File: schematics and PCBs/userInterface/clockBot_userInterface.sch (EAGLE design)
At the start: 7 parts

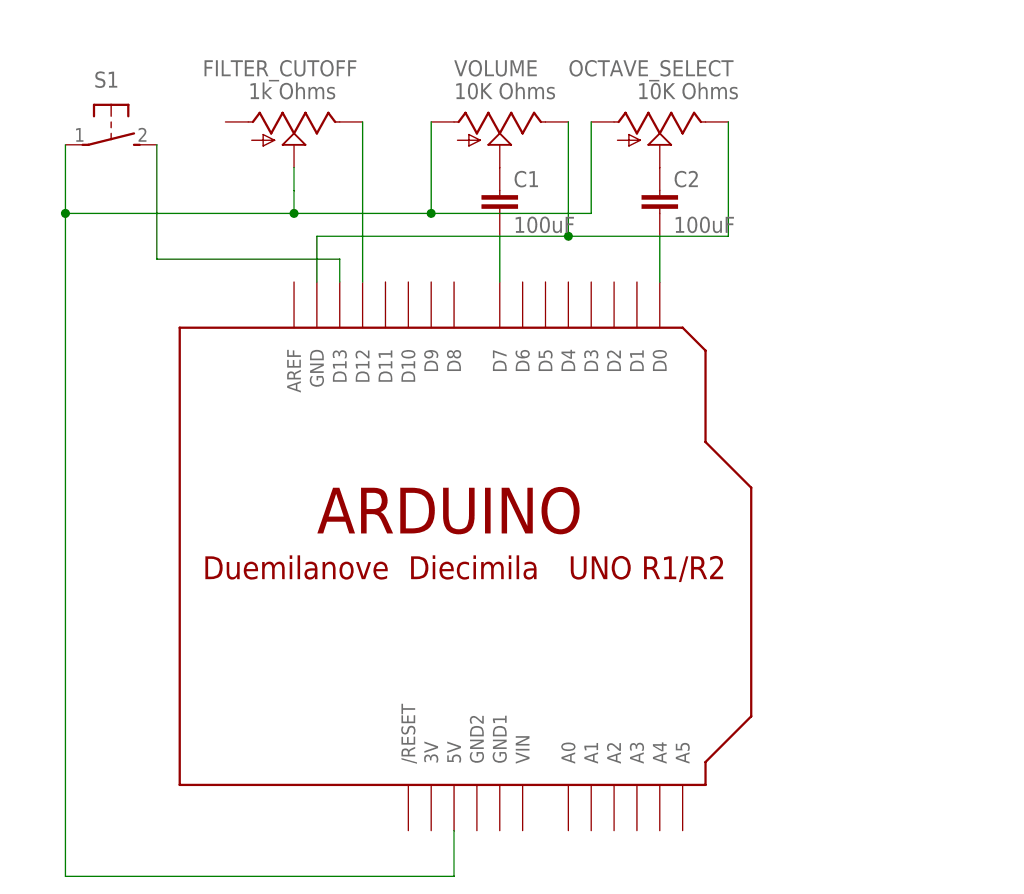
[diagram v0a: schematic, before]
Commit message: organized folders and added erin grace schematic
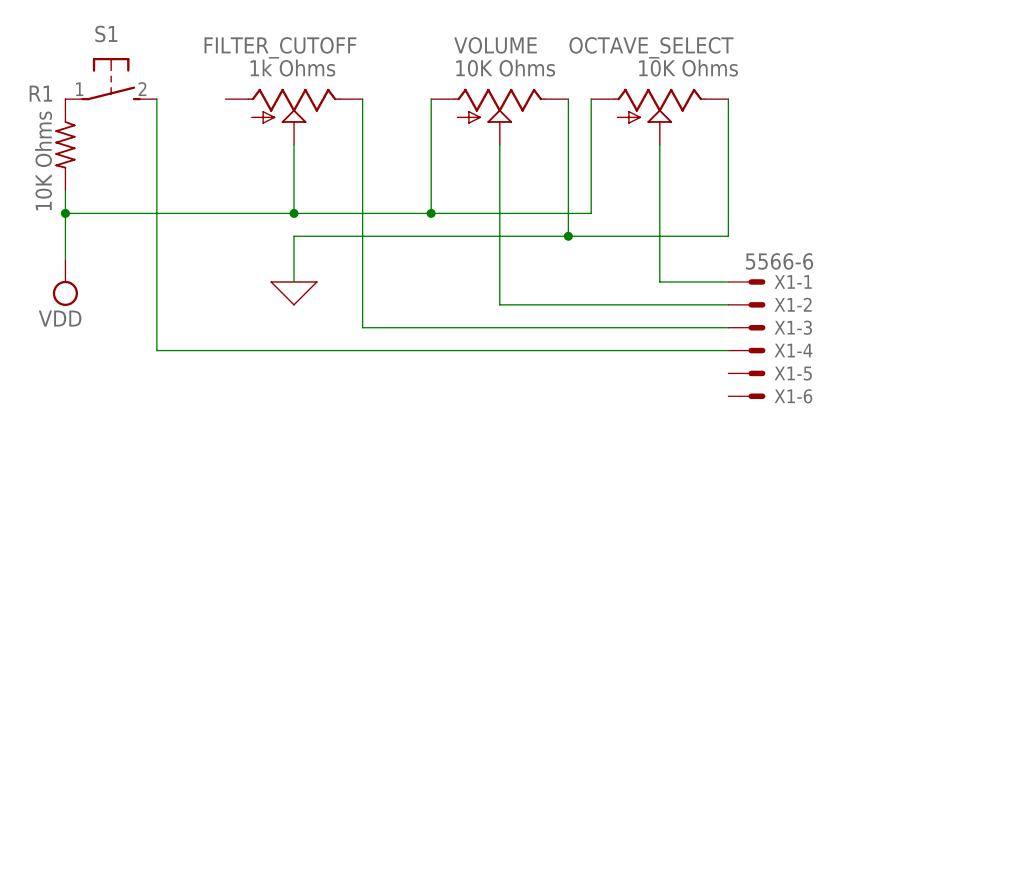
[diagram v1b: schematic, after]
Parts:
- removed C1, C2: 100uF, capacitor-wima:C5/2.5
- removed U$1: ARDUINO-NODIM, adafruit:ARDUINO-NODIM
- added R1: 10K Ohms, adafruit:FLIPFLOP-RES
- added X1: 5566-6, con-molex:5566-6
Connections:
- removed net N$6: C2.1, OCTAVE_SELECT.S
- removed net N$7: C1.1, VOLUME.S
- removed net N$9: OCTAVE_SELECT.E, U$1.GND, VOLUME.E
- new net 0: OCTAVE_SELECT.E, VOLUME.E
- new net VDD: FILTER_CUTOFF.S, OCTAVE_SELECT.A, R1.2, VOLUME.A
- net N$1: now also R1.1; no longer FILTER_CUTOFF.S, OCTAVE_SELECT.A, U$1.5V, VOLUME.A
- net N$10: now also VOLUME.S, X1-2.S; no longer C1.2, U$1.D7
- net N$2: now also X1-4.S; no longer U$1.D13
- net N$3: now also X1-3.S; no longer U$1.D12
- net N$8: now also OCTAVE_SELECT.S, X1-1.S; no longer C2.2, U$1.D0
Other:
- moved on the sheet: FILTER_CUTOFF, OCTAVE_SELECT, S1, VOLUME

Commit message: User interface update
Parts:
- renumbered X1 to INTERFACE
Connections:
- new net N$4: FILTER_CUTOFF.S, INTERFACE-5.S, OCTAVE_SELECT.A, VOLUME.A
- new net N$5: INTERFACE-6.S, OCTAVE_SELECT.E, VOLUME.E
- net 0: now also S1.P; no longer OCTAVE_SELECT.E, VOLUME.E
- net N$1: now also R1.2, S1.S; no longer R1.1, S1.P
- net N$2: now also FILTER_CUTOFF.A; no longer S1.S
- net VDD: now also R1.1; no longer FILTER_CUTOFF.S, OCTAVE_SELECT.A, R1.2, VOLUME.A
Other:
- note added: "5V"
- note added: "F1"
- note added: "F2"
- note added: "GND"
- note added: "Octave"
- note added: "Power Input"
- note added: "Volume"
- moved on the sheet: R1, S1
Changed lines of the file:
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@@
 <part name="OCTAVE_SELECT" library="pot" library_urn="urn:adsk.eagle:library:331" deviceset="TRIM_US-" device="S64W" package3d_urn="urn:adsk.eagle:package:22708/1" value="10K Ohms"/>
 <part name="S1" library="adafruit" library_urn="urn:adsk.eagle:library:420" deviceset="31-XX" device="" package3d_urn="urn:adsk.eagle:package:6240698/1"/>
-<part name="X1" library="con-molex" library_urn="urn:adsk.eagle:library:165" deviceset="5566-6" device="" package3d_urn="urn:adsk.eagle:package:8078581/1"/>
+<part name="INTERFACE" library="con-molex" library_urn="urn:adsk.eagle:library:165" deviceset="5566-6" device="" package3d_urn="urn:adsk.eagle:package:8078581/1"/>
 <part name="SUPPLY1" library="supply2" library_urn="urn:adsk.eagle:library:372" deviceset="VDD" device=""/>
 <part name="X_1" library="ngspice-simulation" library_urn="urn:adsk.eagle:library:527439" deviceset="GND" device=""/>
@@
 <sheet>
 <plain>
+<text x="91.44" y="40.64" size="1.778" layer="91">Octave</text>
+<text x="91.44" y="38.1" size="1.778" layer="91">Volume</text>
+<text x="91.44" y="35.56" size="1.778" layer="91">F1</text>
+<text x="91.44" y="33.02" size="1.778" layer="91">F2</text>
+<text x="91.44" y="30.48" size="1.778" layer="91">5V</text>
+<text x="91.44" y="27.94" size="1.778" layer="91">GND</text>
+<text x="27.94" y="0" size="1.778" layer="91">Power Input</text>
 </plain>
 <instances>
@@
 <attribute name="VALUE" x="60.96" y="63.5" size="1.778" layer="96"/>
 </instance>
-<instance part="S1" gate="1" x="2.54" y="60.96" smashed="yes" rot="R270">
-<attribute name="NAME" x="0.635" y="67.31" size="1.778" layer="95"/>
-<attribute name="VALUE" x="5.715" y="64.77" size="1.778" layer="96"/>
+<instance part="S1" gate="1" x="5.08" y="0" smashed="yes" rot="R270">
+<attribute name="NAME" x="3.175" y="6.35" size="1.778" layer="95"/>
+<attribute name="VALUE" x="8.255" y="3.81" size="1.778" layer="96"/>
 </instance>
-<instance part="X1" gate="-1" x="73.66" y="40.64" smashed="yes">
+<instance part="INTERFACE" gate="-1" x="73.66" y="40.64" smashed="yes">
 <attribute name="NAME" x="76.2" y="39.878" size="1.524" layer="95"/>
 <attribute name="VALUE" x="72.898" y="42.037" size="1.778" layer="96"/>
 </instance>
-<instance part="X1" gate="-2" x="73.66" y="38.1" smashed="yes">
+<instance part="INTERFACE" gate="-2" x="73.66" y="38.1" smashed="yes">
 <attribute name="NAME" x="76.2" y="37.338" size="1.524" layer="95"/>
 </instance>
-<instance part="X1" gate="-3" x="73.66" y="35.56" smashed="yes">
+<instance part="INTERFACE" gate="-3" x="73.66" y="35.56" smashed="yes">
 <attribute name="NAME" x="76.2" y="34.798" size="1.524" layer="95"/>
 </instance>
-<instance part="X1" gate="-4" x="73.66" y="33.02" smashed="yes">
+<instance part="INTERFACE" gate="-4" x="73.66" y="33.02" smashed="yes">
 <attribute name="NAME" x="76.2" y="32.258" size="1.524" layer="95"/>
 </instance>
-<instance part="X1" gate="-5" x="73.66" y="30.48" smashed="yes">
+<instance part="INTERFACE" gate="-5" x="73.66" y="30.48" smashed="yes">
 <attribute name="NAME" x="76.2" y="29.718" size="1.524" layer="95"/>
 </instance>
-<instance part="X1" gate="-6" x="73.66" y="27.94" smashed="yes">
+<instance part="INTERFACE" gate="-6" x="73.66" y="27.94" smashed="yes">
 <attribute name="NAME" x="76.2" y="27.178" size="1.524" layer="95"/>
 </instance>
-<instance part="SUPPLY1" gate="G$1" x="-2.54" y="40.64" smashed="yes" rot="R180">
-<attribute name="VALUE" x="-0.635" y="37.465" size="1.778" layer="96" rot="R180"/>
+<instance part="SUPPLY1" gate="G$1" x="15.24" y="20.32" smashed="yes">
+<attribute name="VALUE" x="13.335" y="26.035" size="1.778" layer="96"/>
 </instance>
-<instance part="X_1" gate="G$1" x="22.86" y="40.64" smashed="yes"/>
-<instance part="R1" gate="G$1" x="-2.54" y="55.88" smashed="yes" rot="R270">
-<attribute name="NAME" x="-3.81" y="62.4586" size="1.778" layer="95" rot="R180"/>
-<attribute name="VALUE" x="-5.842" y="59.69" size="1.778" layer="96" rot="R270"/>
+<instance part="X_1" gate="G$1" x="0" y="-5.08" smashed="yes"/>
+<instance part="R1" gate="G$1" x="15.24" y="10.16" smashed="yes" rot="R270">
+<attribute name="NAME" x="13.97" y="16.7386" size="1.778" layer="95" rot="R180"/>
+<attribute name="VALUE" x="11.938" y="13.97" size="1.778" layer="96" rot="R270"/>
 </instance>
 </instances>
@@
 </busses>
 <nets>
-<net name="N$2" class="0">
-<segment>
-<pinref part="S1" gate="1" pin="S"/>
-<wire x1="7.62" y1="60.96" x2="7.62" y2="33.02" width="0.1524" layer="91"/>
-<pinref part="X1" gate="-4" pin="S"/>
-<wire x1="7.62" y1="33.02" x2="71.12" y2="33.02" width="0.1524" layer="91"/>
-</segment>
-</net>
 <net name="N$3" class="0">
 <segment>
 <pinref part="FILTER_CUTOFF" gate="G$1" pin="E"/>
 <wire x1="30.48" y1="60.96" x2="30.48" y2="35.56" width="0.1524" layer="91"/>
-<pinref part="X1" gate="-3" pin="S"/>
+<pinref part="INTERFACE" gate="-3" pin="S"/>
 <wire x1="30.48" y1="35.56" x2="71.12" y2="35.56" width="0.1524" layer="91"/>
 </segment>
@@
 <net name="N$8" class="0">
 <segment>
-<pinref part="X1" gate="-1" pin="S"/>
+<pinref part="INTERFACE" gate="-1" pin="S"/>
 <wire x1="63.5" y1="40.64" x2="71.12" y2="40.64" width="0.1524" layer="91"/>
 <pinref part="OCTAVE_SELECT" gate="G$1" pin="S"/>
@@
 <net name="N$10" class="0">
 <segment>
-<pinref part="X1" gate="-2" pin="S"/>
+<pinref part="INTERFACE" gate="-2" pin="S"/>
 <wire x1="45.72" y1="38.1" x2="71.12" y2="38.1" width="0.1524" layer="91"/>
 <pinref part="VOLUME" gate="G$1" pin="S"/>
@@
 </segment>
 </net>
-<net name="0" class="0">
+<net name="N$2" class="0">
 <segment>
-<pinref part="VOLUME" gate="G$1" pin="E"/>
-<wire x1="53.34" y1="60.96" x2="53.34" y2="45.72" width="0.1524" layer="91"/>
-<wire x1="53.34" y1="45.72" x2="22.86" y2="45.72" width="0.1524" layer="91"/>
-<pinref part="OCTAVE_SELECT" gate="G$1" pin="E"/>
-<wire x1="71.12" y1="60.96" x2="71.12" y2="45.72" width="0.1524" layer="91"/>
-<wire x1="53.34" y1="45.72" x2="71.12" y2="45.72" width="0.1524" layer="91"/>
-<junction x="53.34" y="45.72"/>
-<pinref part="X_1" gate="G$1" pin="0"/>
-<wire x1="22.86" y1="45.72" x2="22.86" y2="40.64" width="0.1524" layer="91"/>
+<pinref part="FILTER_CUTOFF" gate="G$1" pin="A"/>
+<pinref part="INTERFACE" gate="-4" pin="S"/>
+<wire x1="15.24" y1="60.96" x2="15.24" y2="33.02" width="0.1524" layer="91"/>
+<wire x1="15.24" y1="33.02" x2="71.12" y2="33.02" width="0.1524" layer="91"/>
 </segment>
 </net>
-<net name="N$1" class="0">
-<segment>
-<pinref part="S1" gate="1" pin="P"/>
-<pinref part="R1" gate="G$1" pin="1"/>
-</segment>
-</net>
-<net name="VDD" class="0">
+<net name="N$4" class="0">
 <segment>
 <pinref part="VOLUME" gate="G$1" pin="A"/>
@@
 <pinref part="FILTER_CUTOFF" gate="G$1" pin="S"/>
 <wire x1="22.86" y1="48.26" x2="22.86" y2="55.88" width="0.1524" layer="91"/>
-<wire x1="22.86" y1="48.26" x2="-2.54" y2="48.26" width="0.1524" layer="91"/>
+<pinref part="INTERFACE" gate="-5" pin="S"/>
+<wire x1="22.86" y1="48.26" x2="22.86" y2="30.48" width="0.1524" layer="91"/>
+<wire x1="22.86" y1="30.48" x2="71.12" y2="30.48" width="0.1524" layer="91"/>
 <junction x="22.86" y="48.26"/>
-<pinref part="R1" gate="G$1" pin="2"/>
-<wire x1="-2.54" y1="48.26" x2="-2.54" y2="50.8" width="0.1524" layer="91"/>
-<pinref part="SUPPLY1" gate="G$1" pin="VDD"/>
-<wire x1="-2.54" y1="43.18" x2="-2.54" y2="48.26" width="0.1524" layer="91"/>
-<junction x="-2.54" y="48.26"/>
 </segment>
 </net>
+<net name="N$1" class="0">
+<segment>
+<pinref part="R1" gate="G$1" pin="2"/>
+<wire x1="15.24" y1="5.08" x2="15.24" y2="0" width="0.1524" layer="91"/>
+<pinref part="S1" gate="1" pin="S"/>
+<wire x1="10.16" y1="0" x2="15.24" y2="0" width="0.1524" layer="91"/>
+<wire x1="15.24" y1="0" x2="25.4" y2="0" width="0.1524" layer="91"/>
+<junction x="15.24" y="0"/>
+</segment>
+</net>
+<net name="N$5" class="0">
+<segment>
+<pinref part="VOLUME" gate="G$1" pin="E"/>
+<wire x1="53.34" y1="60.96" x2="53.34" y2="45.72" width="0.1524" layer="91"/>
+<pinref part="OCTAVE_SELECT" gate="G$1" pin="E"/>
+<wire x1="71.12" y1="60.96" x2="71.12" y2="45.72" width="0.1524" layer="91"/>
+<wire x1="53.34" y1="45.72" x2="71.12" y2="45.72" width="0.1524" layer="91"/>
+<pinref part="INTERFACE" gate="-6" pin="S"/>
+<wire x1="53.34" y1="45.72" x2="53.34" y2="27.94" width="0.1524" layer="91"/>
+<wire x1="53.34" y1="27.94" x2="71.12" y2="27.94" width="0.1524" layer="91"/>
+<junction x="53.34" y="45.72"/>
+</segment>
+</net>
+<net name="VDD" class="0">
+<segment>
+<pinref part="R1" gate="G$1" pin="1"/>
+<pinref part="SUPPLY1" gate="G$1" pin="VDD"/>
+<wire x1="15.24" y1="17.78" x2="15.24" y2="15.24" width="0.1524" layer="91"/>
+</segment>
+</net>
+<net name="0" class="0">
+<segment>
+<pinref part="S1" gate="1" pin="P"/>
+<wire x1="0" y1="-5.08" x2="0" y2="0" width="0.1524" layer="91"/>
+<pinref part="X_1" gate="G$1" pin="0"/>
+</segment>
+</net>
